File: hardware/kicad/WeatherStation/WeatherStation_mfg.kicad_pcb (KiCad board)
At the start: 4 copper layers, 100 x 80 mm, 124 parts, among them J1 USB-C, J10 SOIL_TEMP, J11 LEAF_WET, J12 PYRANOMETER, J13 PANEL_TEMP_F, J14 PANEL_TEMP_B, J15 POWER_PULSE, J16 RS485_Bus, J18 SMA_WiFi, J19 RJ45_Magjack, J2 SOLAR_IN, J20 NanoSIM, J21 SMA_LTE, J22 MicroSD, J3 BATTERY, J4 ANEMOMETER, J5 RAIN_GAUGE, J6 SMA_LoRa, J7 DEBUG_UART, J8 SOIL_MOIST_1, J9 SOIL_MOIST_2, Q1 FS8205A, SW1 BOOT, SW2 RESET, SW3 MODE_DIP, U10 STM32F407VGT6, U11 MAX3485ESA+, U12 ATWINC1500, U13 RN4870-I/RM, U14 W5500, U15 SIM7600E-H, U16 TPS7A2033, U2 TP4056, U2A DW01A, U3 AMS1117-3.3, U4 BME280, U5 AS5600, U6 SI1145, U7 BH1750FVI, U8 SX1276/RFM95W, Y1 8MHz, Y2 25MHz

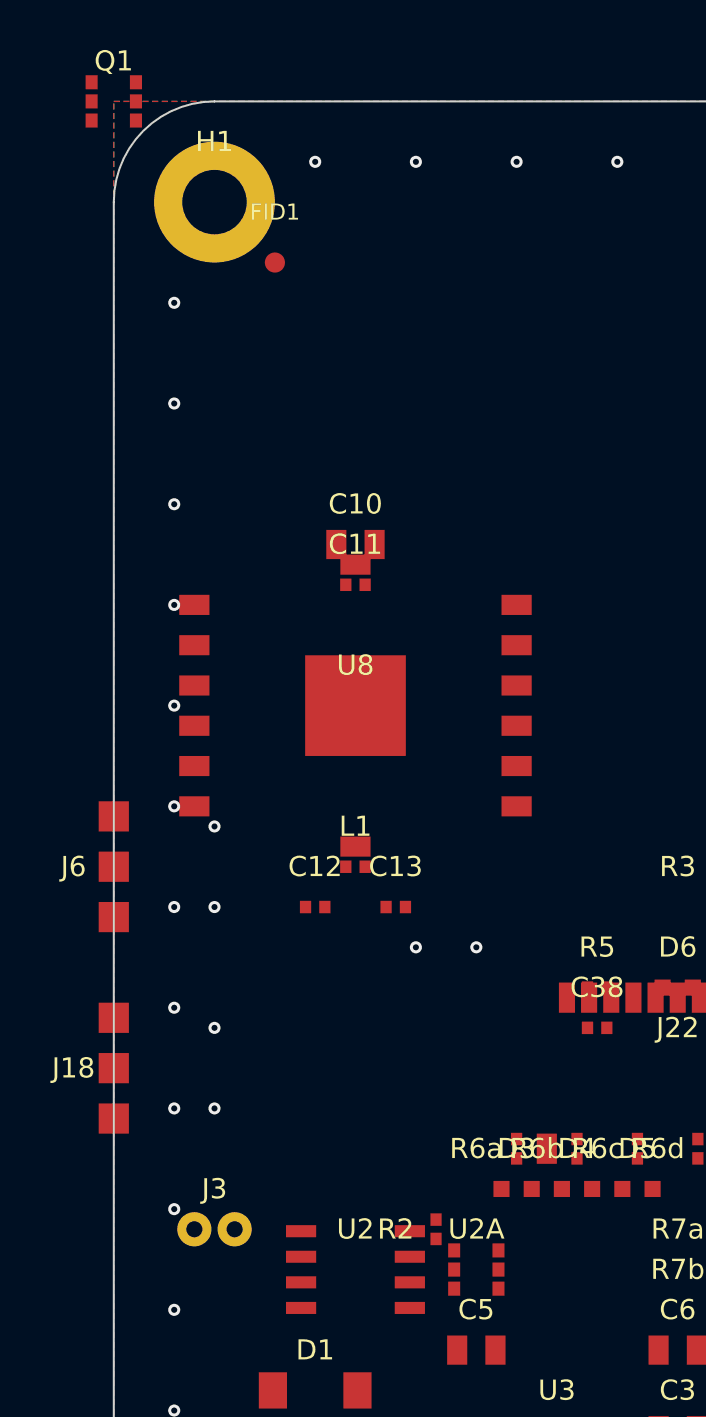
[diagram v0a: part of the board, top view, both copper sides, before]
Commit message: fix: correct net_label→label and comma in coordinates for KiCad
- communication.kicad_sch: replaced 12 instances of invalid `net_label`
  keyword with `label` (valid KiCad schematic syntax)
- WeatherStation_mfg.kicad_pcb: fixed `(at 22, 58)` → `(at 22 58)`,
  commas are not valid separators in S-expressions

https://claude.ai/code/session_01XHnfZQ5BbxTCTBMCteQyVe
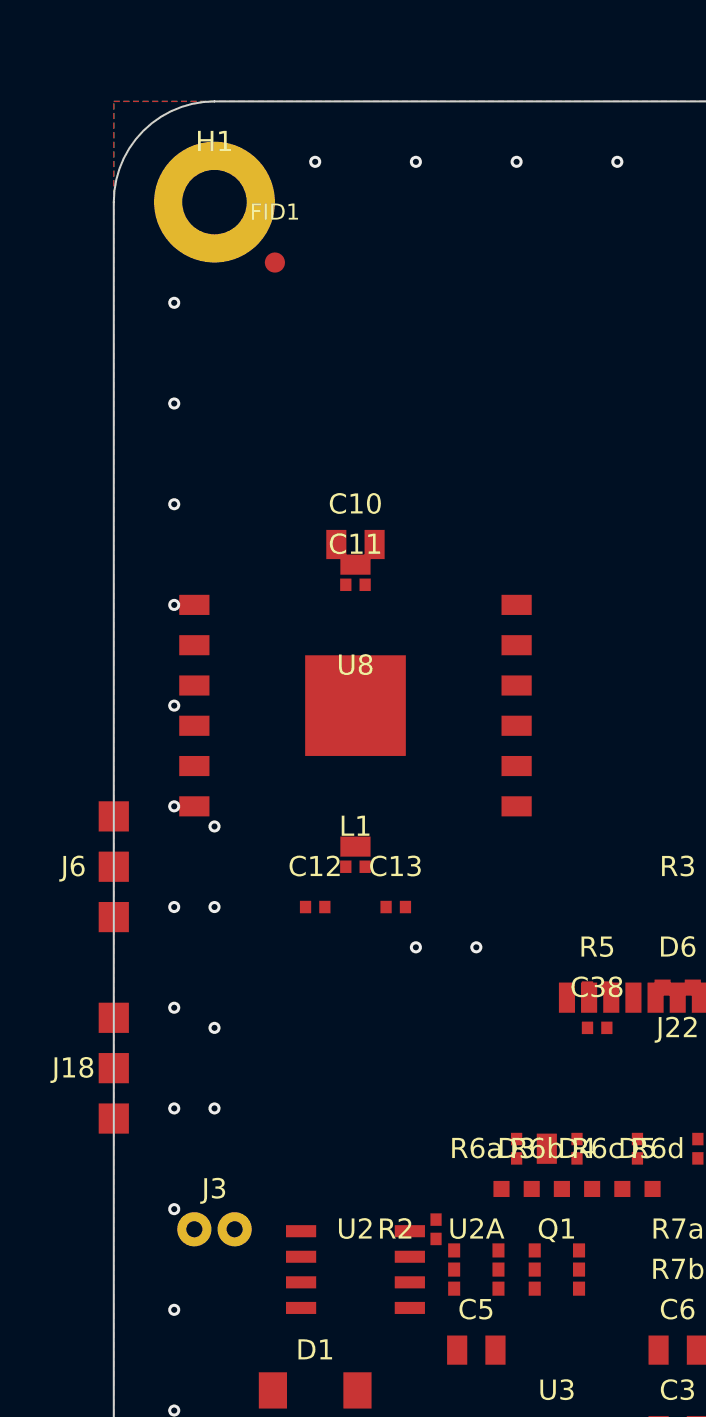
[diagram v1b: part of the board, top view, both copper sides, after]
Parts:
- moved Q1 22.0 mm to (22.0, 58.0)
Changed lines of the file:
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@@
   (footprint "Package_SO:SOT-23-6" (layer "F.Cu")
     (tstamp "fp-q1-0001")
-    (at 22, 58)
+    (at 22 58)
     (property "Reference" "Q1" (at 0 -2) (layer "F.SilkS") (effects (font (size 1 1) (thickness 0.15))))
     (property "Value" "FS8205A" (at 0 2) (layer "F.Fab") (effects (font (size 1 1) (thickness 0.15))))
